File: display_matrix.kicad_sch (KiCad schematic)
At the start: 19 parts, among them U1 LSHD-5503, U2 LSHD-5503, U3 LSHD-5503, U4 LSHD-5503, U6 LSHD-5503, U7 SN74LVC244A

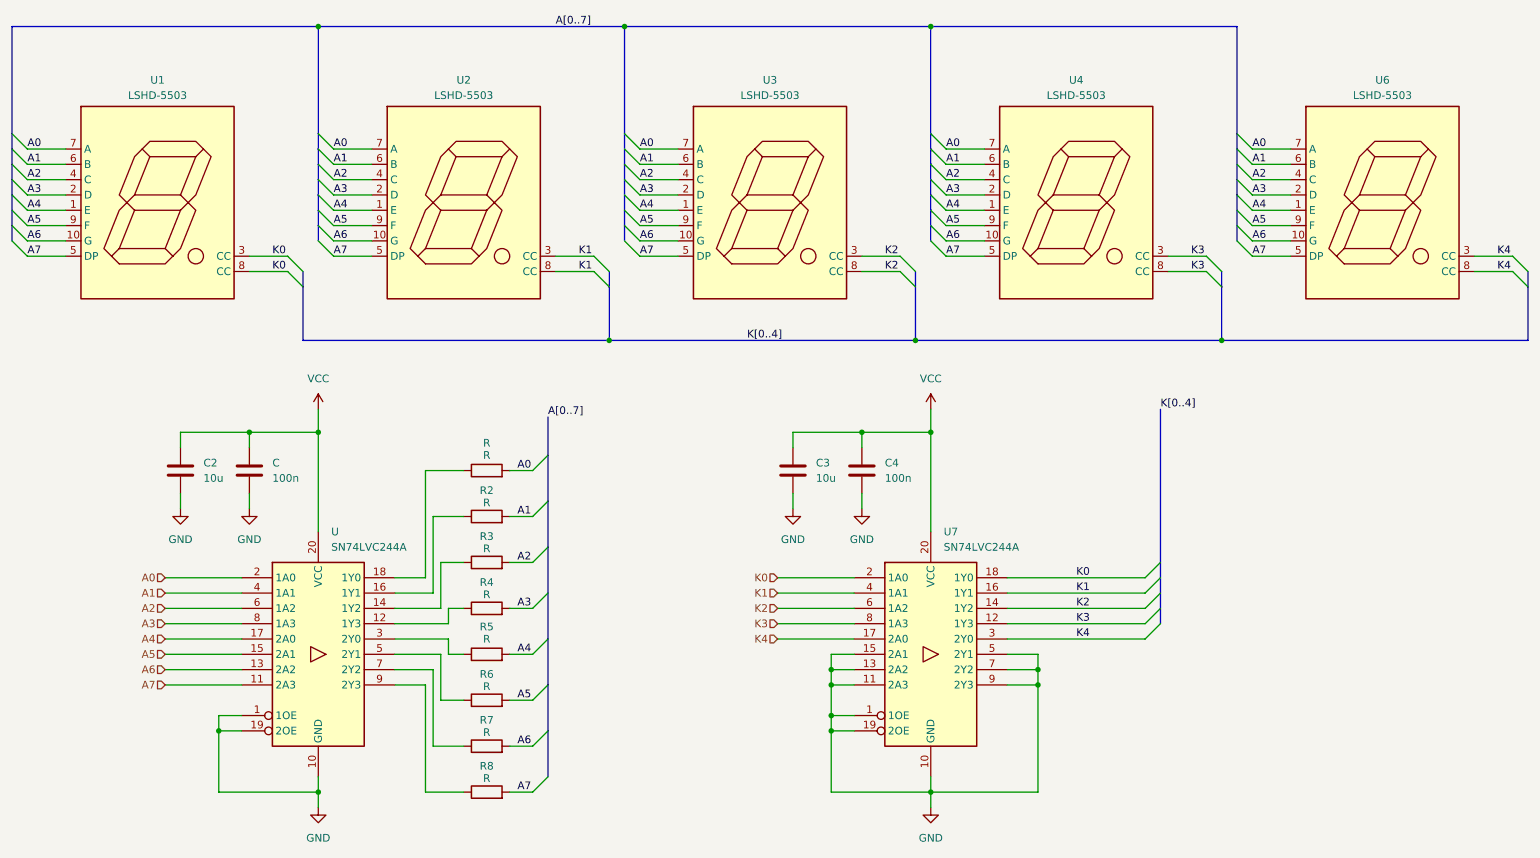
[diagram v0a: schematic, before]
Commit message: - addition of sensors - addition of GPS - inprogress power circuitary
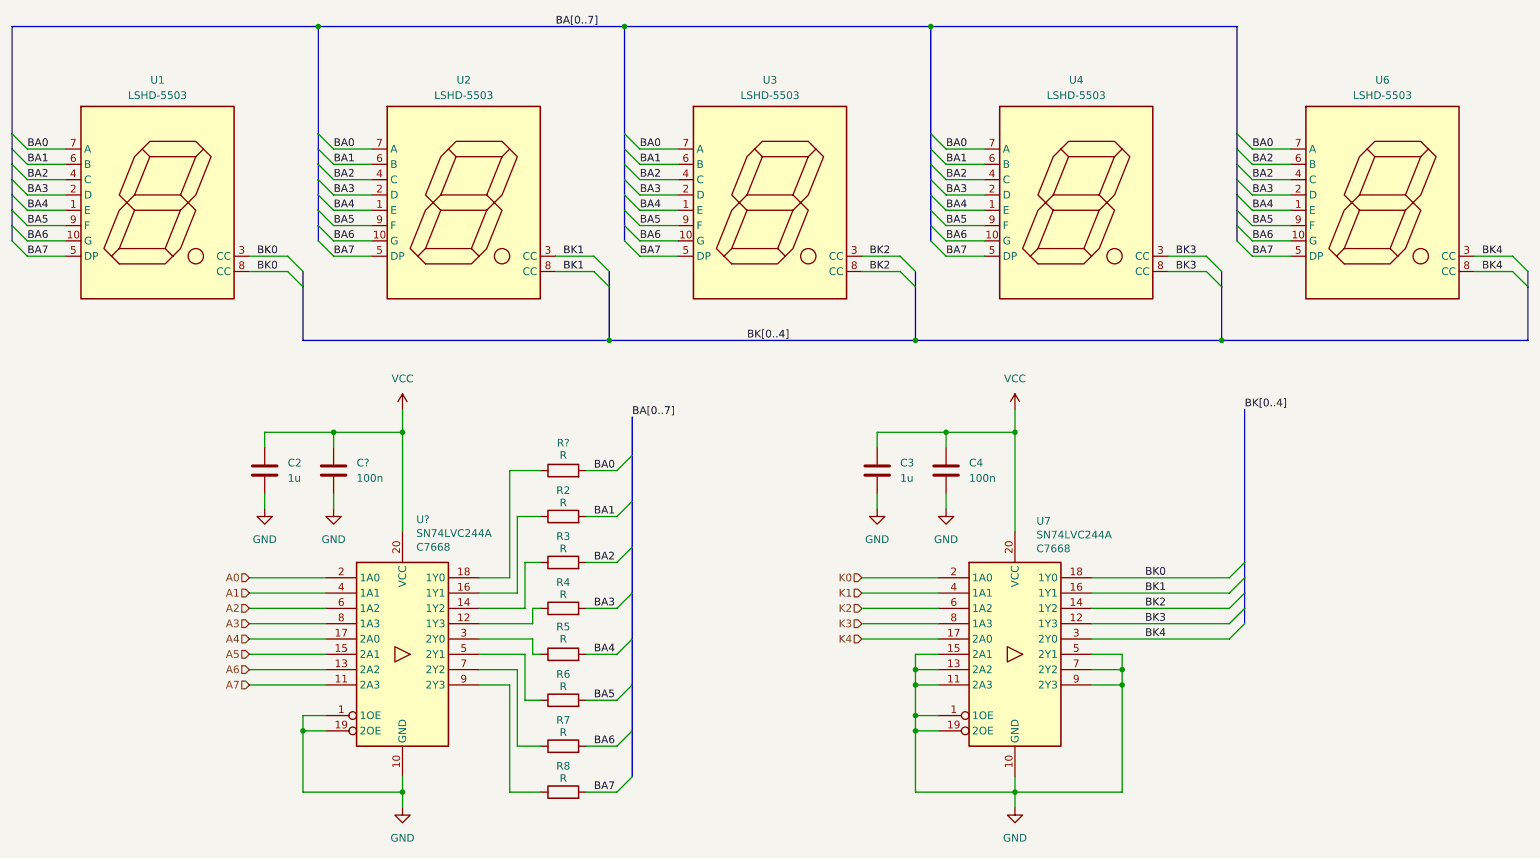
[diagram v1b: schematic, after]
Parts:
- C2, C3: value 10u -> 1u
- U7: LCSC (none) -> C7668
- U?: renamed from U; LCSC (none) -> C7668
- renumbered C to C?, R to R?
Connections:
- net A0: no longer R?.2, U1.7 (A), U2.7 (A), U3.7 (A), U4.7 (A), U6.7 (A)
- net A1: no longer R2.2, U1.6 (B), U2.6 (B), U3.6 (B), U4.6 (B), U6.6 (B)
- net A2: no longer R3.2, U1.4 (C), U2.4 (C), U3.4 (C), U4.4 (C), U6.4 (C)
- net A3: no longer R4.2, U1.2 (D), U2.2 (D), U3.2 (D), U4.2 (D), U6.2 (D)
- net A4: no longer R5.2, U1.1 (E), U2.1 (E), U3.1 (E), U4.1 (E), U6.1 (E)
- net A5: no longer R6.2, U1.9 (F), U2.9 (F), U3.9 (F), U4.9 (F), U6.9 (F)
- net A6: no longer R7.2, U1.10 (G), U2.10 (G), U3.10 (G), U4.10 (G), U6.10 (G)
- net A7: no longer R8.2, U1.5 (DP), U2.5 (DP), U3.5 (DP), U4.5 (DP), U6.5 (DP)
- net K0: no longer U1.3 (CC), U1.8 (CC), U7.18 (1Y0)
- net K1: no longer U2.3 (CC), U2.8 (CC), U7.16 (1Y1)
- net K2: no longer U3.3 (CC), U3.8 (CC), U7.14 (1Y2)
- net K3: no longer U4.3 (CC), U4.8 (CC), U7.12 (1Y3)
- net K4: no longer U6.3 (CC), U6.8 (CC), U7.3 (2Y0)
- new net BA0: R?.2, U1.7 (A), U2.7 (A), U3.7 (A), U4.7 (A), U6.7 (A)
- new net BA1: R2.2, U1.6 (B), U2.6 (B), U3.6 (B), U4.6 (B)
- new net BA2: R3.2, U1.4 (C), U2.4 (C), U3.4 (C), U4.4 (C), U6.4 (C), U6.6 (B)
- new net BA3: R4.2, U1.2 (D), U2.2 (D), U3.2 (D), U4.2 (D), U6.2 (D)
- new net BA4: R5.2, U1.1 (E), U2.1 (E), U3.1 (E), U4.1 (E), U6.1 (E)
- new net BA5: R6.2, U1.9 (F), U2.9 (F), U3.9 (F), U4.9 (F), U6.9 (F)
- new net BA6: R7.2, U1.10 (G), U2.10 (G), U3.10 (G), U4.10 (G), U6.10 (G)
- new net BA7: R8.2, U1.5 (DP), U2.5 (DP), U3.5 (DP), U4.5 (DP), U6.5 (DP)
- new net BK0: U1.3 (CC), U1.8 (CC), U7.18 (1Y0)
- new net BK1: U2.3 (CC), U2.8 (CC), U7.16 (1Y1)
- new net BK2: U3.3 (CC), U3.8 (CC), U7.14 (1Y2)
- new net BK3: U4.3 (CC), U4.8 (CC), U7.12 (1Y3)
- new net BK4: U6.3 (CC), U6.8 (CC), U7.3 (2Y0)
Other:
- moved on the sheet: C2, C3, C4, C?, R2, R3, R4, R5, R6, R7, R8, R?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
